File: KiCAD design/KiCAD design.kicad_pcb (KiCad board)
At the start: 2 copper layers, 94 x 84 mm, 31 parts, among them J201 Conn_02x19_Odd_Even, J202 Conn_01x03_Female, J203 Conn_01x03_Female, J204 Conn_02x19_Odd_Even, J205 JST BATTERY, J206 JST SENS TOF 2, J208 JST SENS TOF 1, J401 Conn_02x06_Top_Bottom, U101 NUCLEO64-F411RE, U301 MCP1804T, U302 MIC5317, U401 ACS712xLCTR-20A

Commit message: end PCB
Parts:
- moved U101 97.4 mm to (150.0, 67.0)
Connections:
- J201 pad 16: unconnected-(J201-Pad16) -> /CONNECTORS/BT_3.3V
- J401 pad 8: /CONNECTORS/RST_N -> +3.3V
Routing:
- net /CONNECTORS/Bluetooth_TX: track 0.00 -> 72.7 mm
- net +12V: track 93.5 -> 112.7 mm
- net /CONNECTORS/TOF1_SDA: track 57.5 -> 62.3 mm
- net +3.3V: track 71.9 -> 76.0 mm, vias 0 -> 1
- net /CONNECTORS/TOF1_DATA_READY: track 46.2 -> 50.2 mm
- net +5V: track 178.5 -> 181.7 mm, vias 1 -> 2
- net /CONNECTORS/Bluetooth_RX: track 36.8 -> 39.2 mm
- net GND: track 2.01 -> 3.53 mm, vias 1 -> 2
- net /CONNECTORS/TOF2_SCL: track 69.7 -> 70.6 mm, vias 1 -> 2
- net /ON_BOARD_COMPONENTS/IP+: track 20.7 -> 21.4 mm
- net /CONNECTORS/TOF1_SCL: track 52.6 -> 52.9 mm, vias 1 -> 2

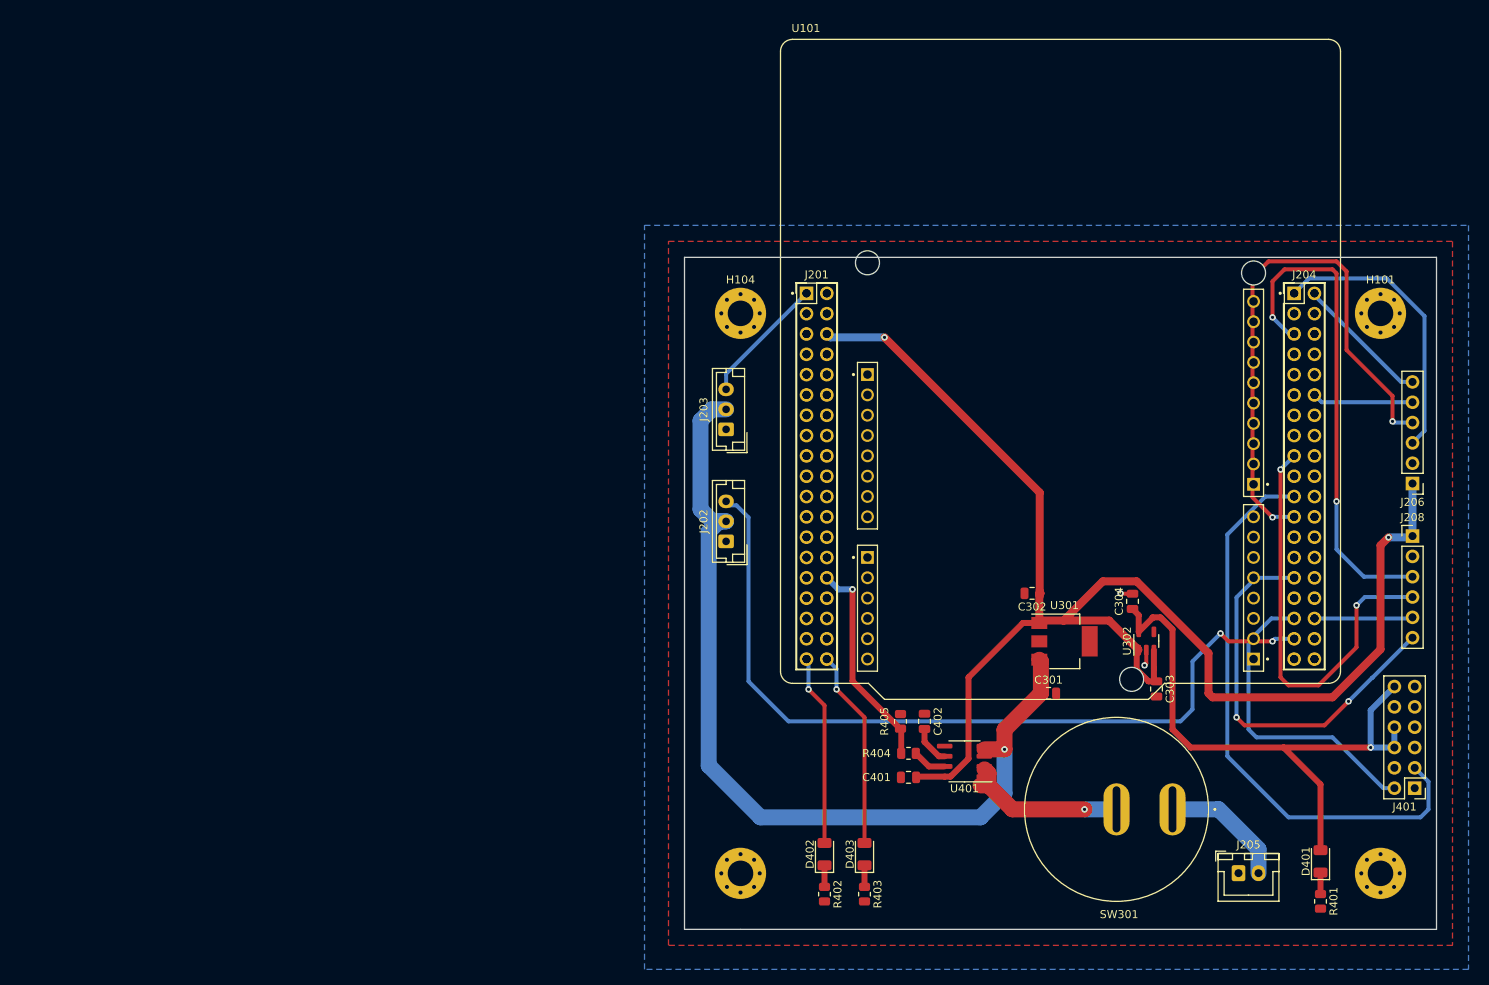
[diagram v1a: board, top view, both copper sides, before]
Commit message: KiCAD widening of copper pads
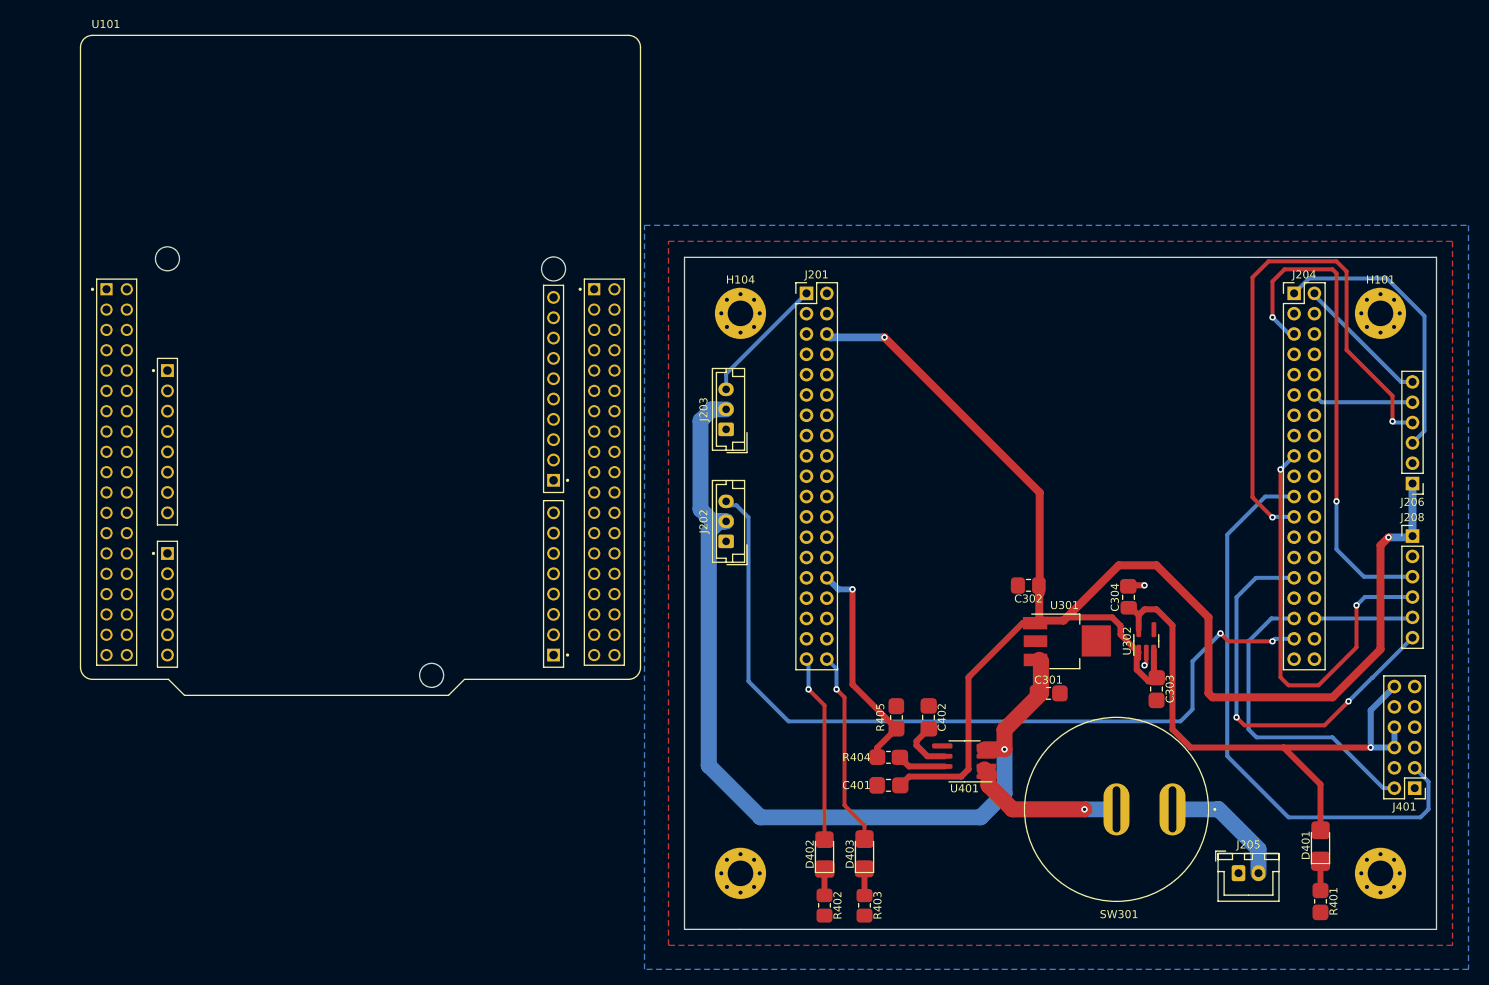
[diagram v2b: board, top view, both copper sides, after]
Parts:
- moved U101 87.5 mm to (62.5, 66.5)
- moved C401 2.69 mm to (128.5, 119.0)
- moved R404 2.55 mm to (128.5, 115.5)
- moved D401 2.00 mm to (182.5, 126.5)
- moved R402 1.40 mm to (120.5, 134.0)
- moved R403 1.40 mm to (125.5, 134.0)
- moved C302 1.10 mm to (146.0, 94.0)
- moved C304 0.71 mm to (158.5, 95.5)
- moved C402 0.71 mm to (133.5, 110.5)
- moved R405 0.71 mm to (129.5, 110.5)
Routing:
- net +5V: track 181.7 -> 190.0 mm
- net +3.3V: track 76.0 -> 73.6 mm
- net Net-(C402-Pad2): track 4.89 -> 6.81 mm
- net Net-(R404-Pad1): track 4.29 -> 6.07 mm
- net /CONNECTORS/CURRENT_MEASURE: track 26.9 -> 28.1 mm
- net Net-(D403-Pad1): track 2.69 -> 3.78 mm
- net Net-(D402-Pad1): track 2.69 -> 3.75 mm
- net /ON_BOARD_COMPONENTS/IP+: track 21.4 -> 20.4 mm
- net Net-(D401-Pad1): track 2.69 -> 3.66 mm
- net GND: track 3.53 -> 4.08 mm

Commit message: Modified PCB
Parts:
- removed U101: NUCLEO64-F411RE, NUCLEO.lib:ST_NUCLEO-F401RE
- H101: footprint MountingHole:MountingHole_3.2mm_M3_Pad_Via -> MountingHole:MountingHole_4.3mm_M4_DIN965_Pad; moved to B.Cu
- H102, H103, H104: footprint MountingHole:MountingHole_3.2mm_M3_Pad_Via -> MountingHole:MountingHole_4.3mm_M4_DIN965_Pad
- J205: footprint Connector_JST:JST_XH_B2B-XH-A_1x02_P2.50mm_Vertical -> Connector_AMASS:AMASS_XT60-M_1x02_P7.20mm_Vertical
- moved J205 3.42 mm to (175.0, 132.0), turned to 90 degrees
- moved H102 2.83 mm to (108.0, 132.0)
- moved H103 2.83 mm to (192.0, 132.0)
- moved H101 2.00 mm to (192.0, 60.0), turned to 180 degrees
- moved H104 2.00 mm to (108.0, 60.0)
- moved D401 1.51 mm to (184.0, 126.3)
- moved R401 1.51 mm to (184.0, 133.3)
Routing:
- net /CONNECTORS/USART_HD_ARM: track 103.0 -> 110.3 mm
- net /CONNECTORS/TOF2_SDA: track 35.5 -> 40.2 mm
- net /CONNECTORS/BATT: track 15.8 -> 12.2 mm
- net /CONNECTORS/Bluetooth_TX: track 72.7 -> 70.6 mm
- net /CONNECTORS/TOF2_DATA_READY: track 17.0 -> 17.9 mm
- net +3.3V: track 73.6 -> 73.1 mm
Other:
- board size 94 x 84 mm -> 96 x 86 mm

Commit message: Updated PCB and GRB files
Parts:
- H101: moved to F.Cu
- moved J202 20.5 mm to (108.2, 109.0)
- moved J203 20.5 mm to (108.2, 95.0)
- moved C304 3.52 mm to (161.8, 94.2)
- moved SW301 2.83 mm to (155.0, 124.0)
- moved D402 2.00 mm to (118.5, 127.6)
- moved R402 2.00 mm to (118.5, 134.0)
- moved D403 1.50 mm to (124.0, 127.6)
- moved R403 1.50 mm to (124.0, 134.0)
- moved C301 0.90 mm to (149.4, 107.5)
- moved C303 0.80 mm to (161.5, 107.6)
- turned H101 to 0 degrees
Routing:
- net /CONNECTORS/USART_HD_BASE: track 16.2 -> 39.6 mm
- net /CONNECTORS/USART_HD_ARM: track 110.3 -> 88.3 mm
- net +12V: track 112.7 -> 95.4 mm
- net +5V: track 190.0 -> 198.6 mm
- net /CONNECTORS/TOF2_SCL: track 70.6 -> 74.5 mm
- net GND: track 4.08 -> 1.92 mm, vias 2 -> 1
- net /CONNECTORS/Bluetooth_TX: track 70.6 -> 72.8 mm
- net /CONNECTORS/BATT: track 12.2 -> 14.3 mm
- net /ON_BOARD_COMPONENTS/IP+: track 20.4 -> 19.1 mm
- net /CONNECTORS/LED2: track 23.9 -> 22.7 mm
- net /CONNECTORS/TOF1_DATA_READY: track 50.2 -> 49.0 mm
- net /CONNECTORS/LED1: track 24.9 -> 23.8 mm
- net /CONNECTORS/CURRENT_MEASURE: track 28.1 -> 28.9 mm
- net Net-(C402-Pad2): track 6.81 -> 7.38 mm
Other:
- board size 96 x 86 mm -> 96.8 x 86.2 mm
- board text added: "ESP GROUP 2"
